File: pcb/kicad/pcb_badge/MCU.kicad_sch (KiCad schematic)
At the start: 58 parts, among them J3 Conn_01x04_Pin, J4 Conn_01x03_Pin, J5 Conn_01x03_Pin, J7 Conn_01x02_Pin, Q9 2N7002, SW1 SW_MEC_5E, SW2 SW_MEC_5E, SW3 SW_MEC_5E, SW4 SW_MEC_5E, SW5 SW_MEC_5E, SW6 SW_MEC_5E, SW7 SW_MEC_5E, SW8 SW_MEC_5E, U3 STM32F103CBT6, U6 IRM-H638T/TR2, Y1 TAXM8M4RFDCET2T

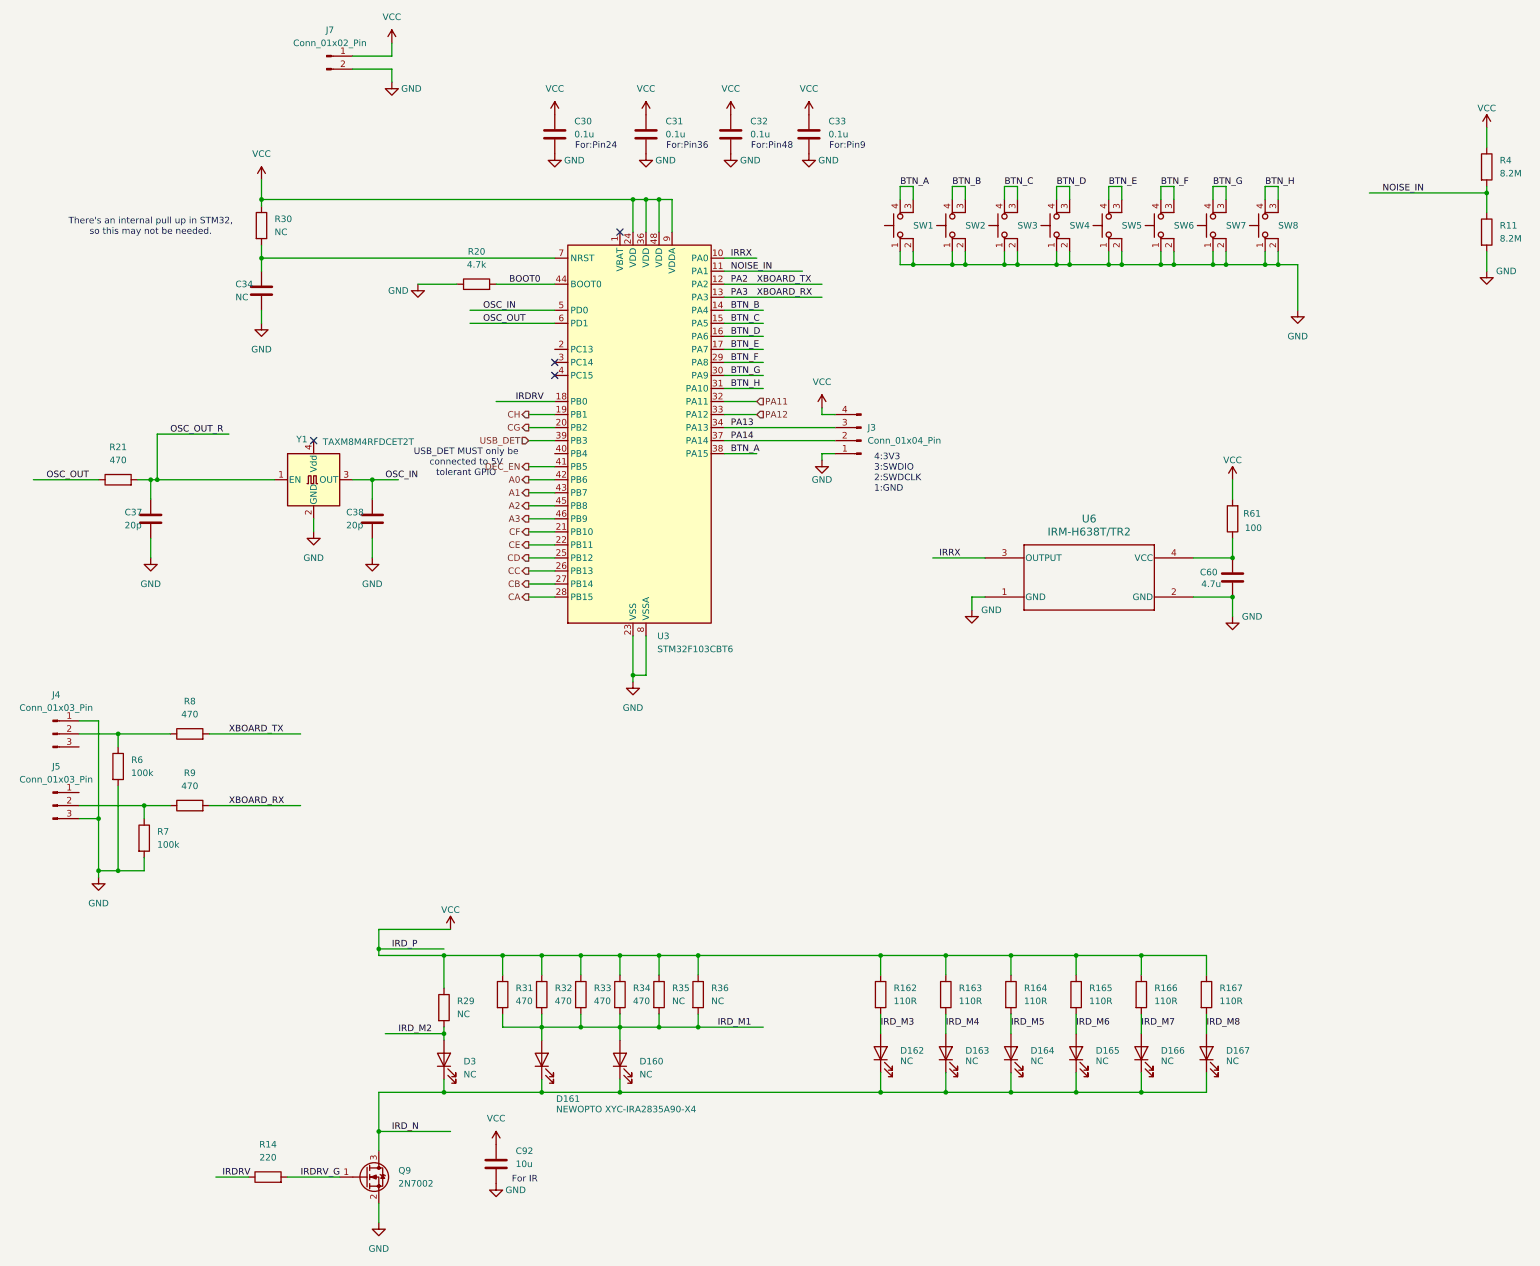
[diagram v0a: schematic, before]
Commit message: add accelerometer
1. change LedA1, A0 pin connection
2. add I2C1, U5 LSM6DS3TR-C
3. disconnect USB_DET
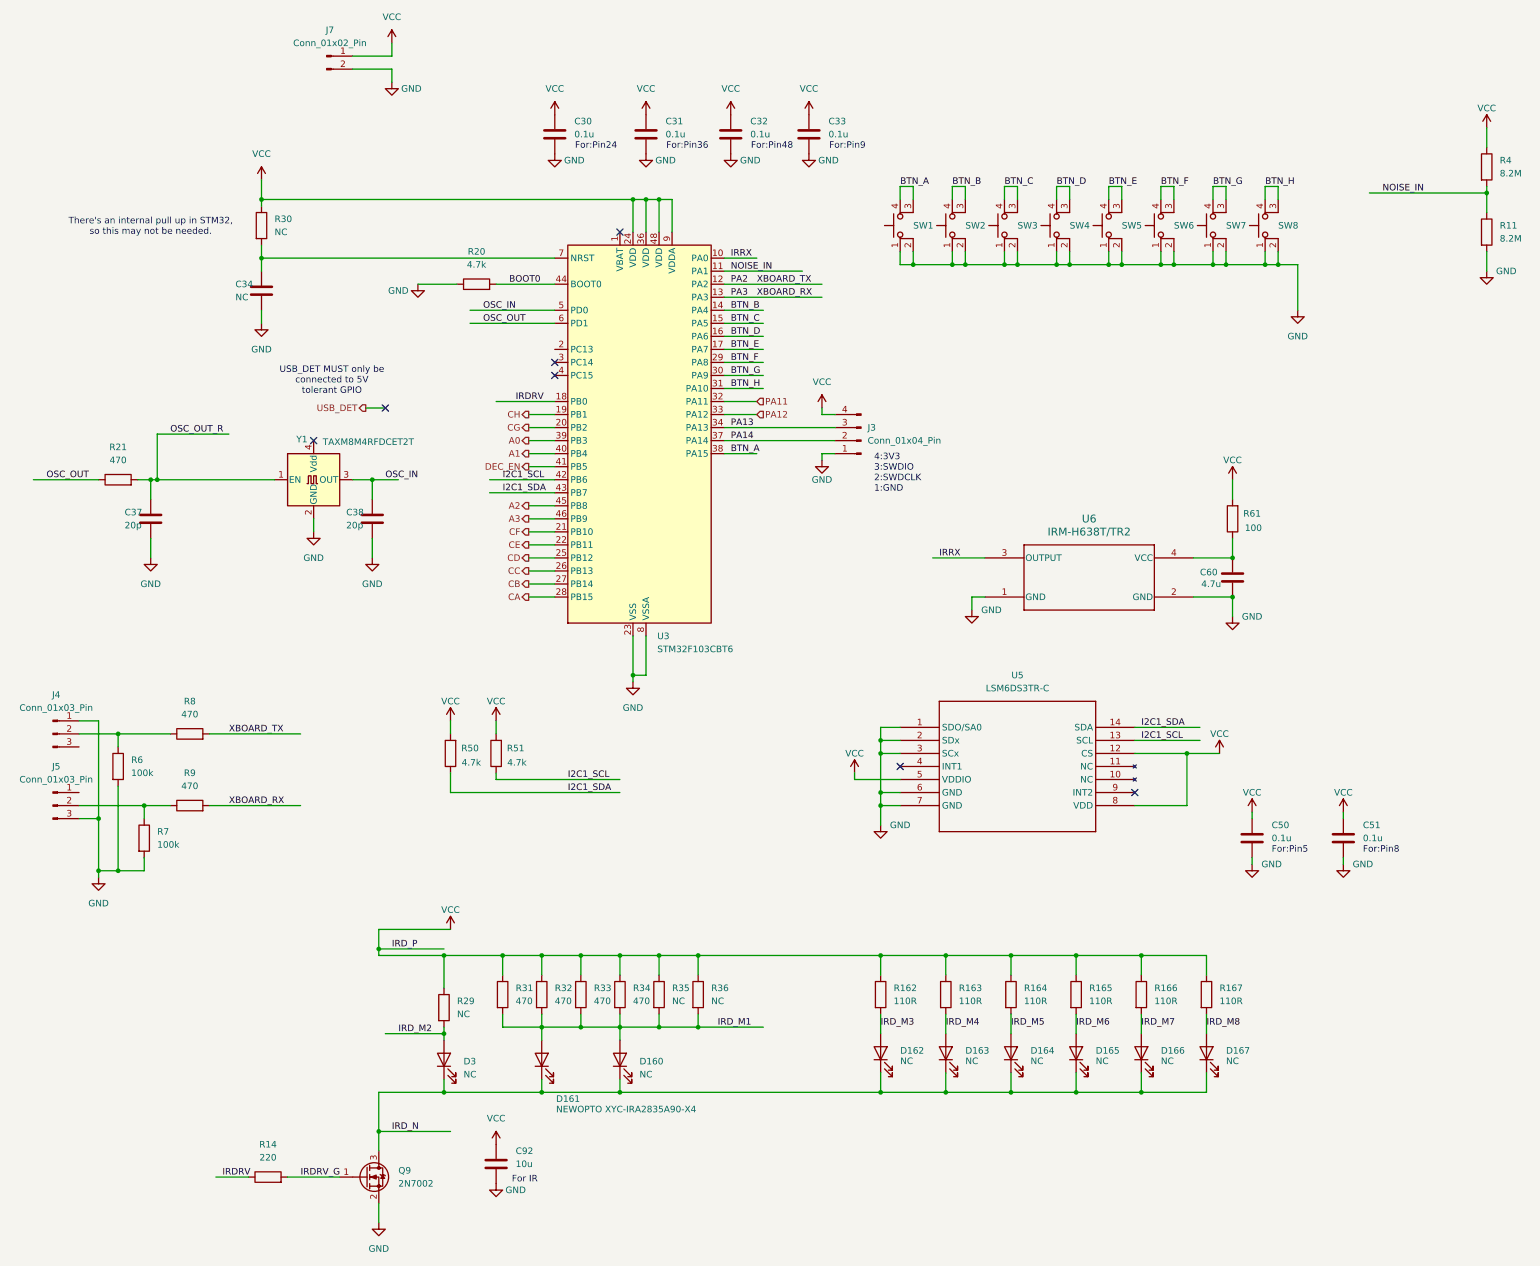
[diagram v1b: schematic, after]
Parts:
- added C50, C51: 0.1u, Capacitor_SMD:C_0402_1005Metric_Pad0.74x0.62mm_HandSolder, symbol Device:C
- added R50, R51: 4.7k, Resistor_SMD:R_0402_1005Metric_Pad0.72x0.64mm_HandSolder, symbol Device:R
- added U5: LSM6DS3TR-C, myLib:QFN_S3TR-C_STM, symbol myLib:LSM6DS3TR-C
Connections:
- net A0: now also U3.39 (PB3); no longer U3.42 (PB6)
- net A1: now also U3.40 (PB4); no longer U3.43 (PB7)
- net GND: now also C50.2, C51.2, U5.1 (SDO/SA0), U5.2 (SDx), U5.3 (SCx), U5.6 (GND), U5.7 (GND)
- net USB_DET: no longer U3.39 (PB3)
- net VCC: now also C50.1, C51.1, R50.2, R51.2, U5.12 (CS), U5.5 (VDDIO), U5.8 (VDD)
- new net I2C1_SCL: R51.1, U3.42 (PB6), U5.13 (SCL)
- new net I2C1_SDA: R50.1, U3.43 (PB7), U5.14 (SDA)
- no-connect marks 4 -> 7
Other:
- note added: "For:Pin5"
- note added: "For:Pin8"
